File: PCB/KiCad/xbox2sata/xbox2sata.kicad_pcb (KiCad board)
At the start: 4 copper layers, 33 x 58.9 mm, 47 parts, among them J1 929975-01-20-RK, J2 61203921621, J3 SATA-A-PL-SMT-K, U1 1V2 voltage regulator, U5 88SA8052, Y1 25MHz

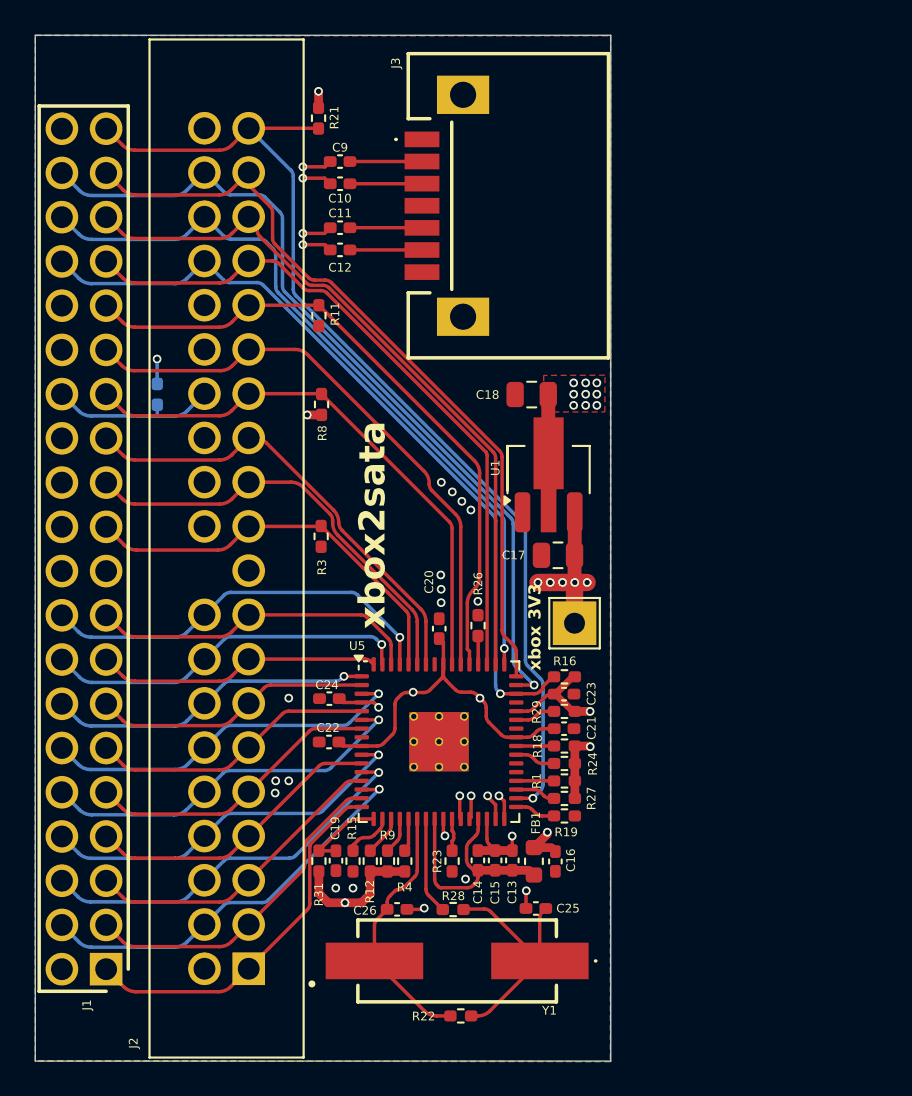
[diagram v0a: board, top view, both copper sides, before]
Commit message: Two resistors removed, two component values changed
R27 : T2
Not installed, removed

R1 : T3
From 4.7K to 10K

R24 : T6
Not installed, removed

R31 change from 5.6K to 1M
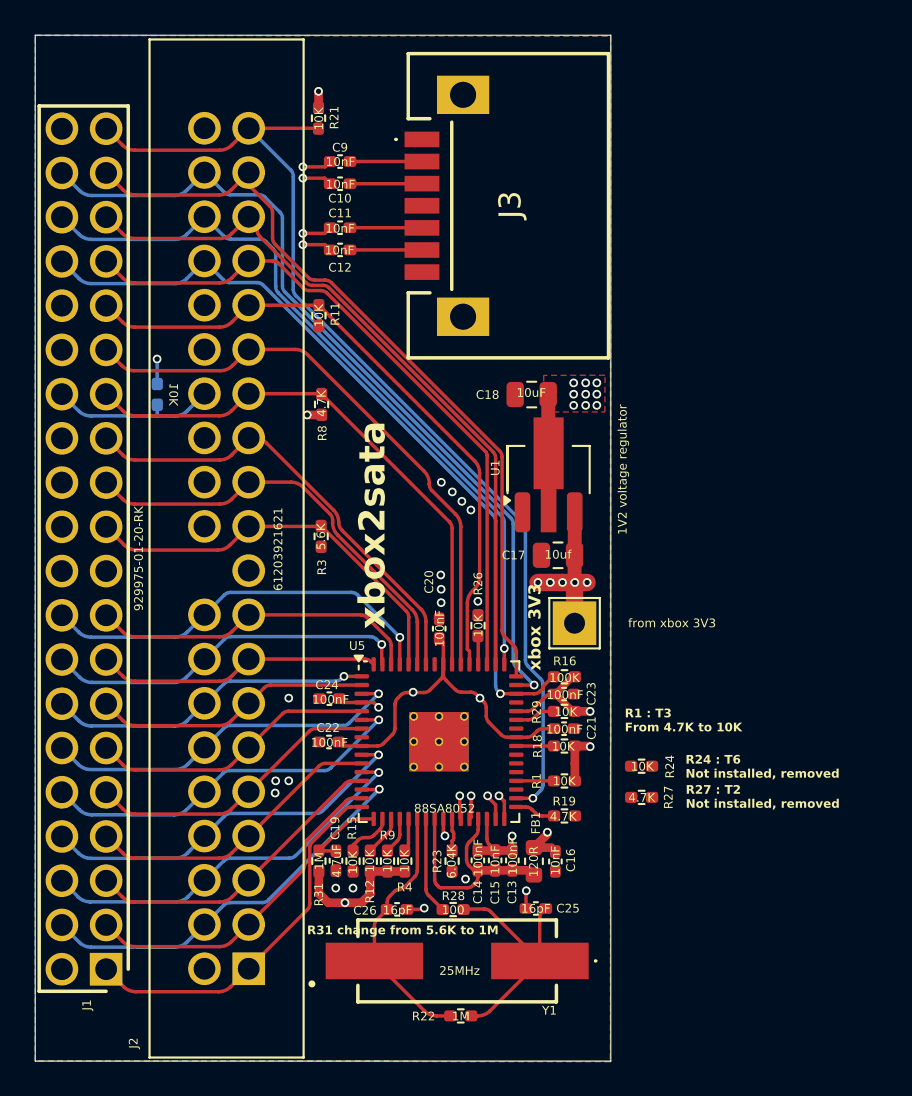
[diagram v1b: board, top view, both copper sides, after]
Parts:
- R1: value 4.7K -> 10K
- R31: value 5.6K -> 1M
- moved R27 4.43 mm to (138.9, 100.6)
- moved R24 4.43 mm to (138.9, 98.8)
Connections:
- R24 pad 1: +3V3 -> unconnected-(R24-Pad1)
- R24 pad 2: T6 -> unconnected-(R24-Pad2)
- R27 pad 1: T2 -> unconnected-(R27-Pad1)
- R27 pad 2: +3V3 -> unconnected-(R27-Pad2)
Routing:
- net T2: track 2.33 -> 0.00 mm
- net T6: track 2.33 -> 0.00 mm
- net +3V3: track 35.7 -> 34.7 mm
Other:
- board text added: "R1 : T3 From 4.7K to 10K"
- board text added: "R24 : T6 Not installed, removed"
- board text added: "R27 : T2 Not installed, removed"
- board text added: "R31 change from 5.6K to 1M"
